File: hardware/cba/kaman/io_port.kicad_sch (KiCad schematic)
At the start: 0 parts

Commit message: hw(schematic): USB to UART circuit for ESP32
With CH340C the UBS to UART for programming the ESP32 is done and it has
the ESD protection with the type C port and the VBUS on USB isn't used
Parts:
- added C10: 100nF, Capacitor_SMD:C_0402_1005Metric_Pad0.74x0.62mm_HandSolder, symbol Device:C
- added C13: 100nF, symbol Device:C
- added J4: USB_C_Receptacle_USB2.0_16P, Connector_USB:USB_C_Receptacle_G-Switch_GT-USB-7010ASV, symbol Connector:USB_C_Receptacle_USB2.0_16P
- added R11, R12: 5.1K, symbol Device:R_US
- added U6: CH340C, Package_SO:SOIC-16_3.9x9.9mm_P1.27mm, symbol Interface_USB:CH340C
- added U7: PRTR5V0U2D, Package_TO_SOT_SMD:SOT-666, symbol Power_Protection:USBLC6-2P6
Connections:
- new net: J4.B5 (CC2), R11.2
- new net: U6.5 (UD+), U7.1 (I/O1)
- new net: U6.6 (UD-), U7.3 (I/O2)
- new net: J4.A6 (D+), J4.B6 (D+), U7.4 (I/O2)
- new net: J4.A7 (D-), J4.B7 (D-), U7.6 (I/O1)
- new net: J4.A4 (VBUS), J4.A9 (VBUS), J4.B4 (VBUS), J4.B9 (VBUS)
- new net: J4.A5 (CC1), R12.2
- new net +3.3V: C10.2, C13.1, U6.16 (VCC), U6.4 (V3), U7.5 (VBUS)
- new net DTR: U6.13 (~{DTR})
- new net GND: C10.1, C13.2, J4.A1 (GND), J4.A12 (GND), J4.B1 (GND), J4.B12 (GND), J4.S1 (SHIELD), R11.1, R12.1, U6.1 (GND), U7.2 (GND)
- new net RTS: U6.14 (~{RTS})
- new net UART RX: U6.2 (TXD)
- new net UART TX: U6.3 (RXD)
- no-connect marks 0 -> 8

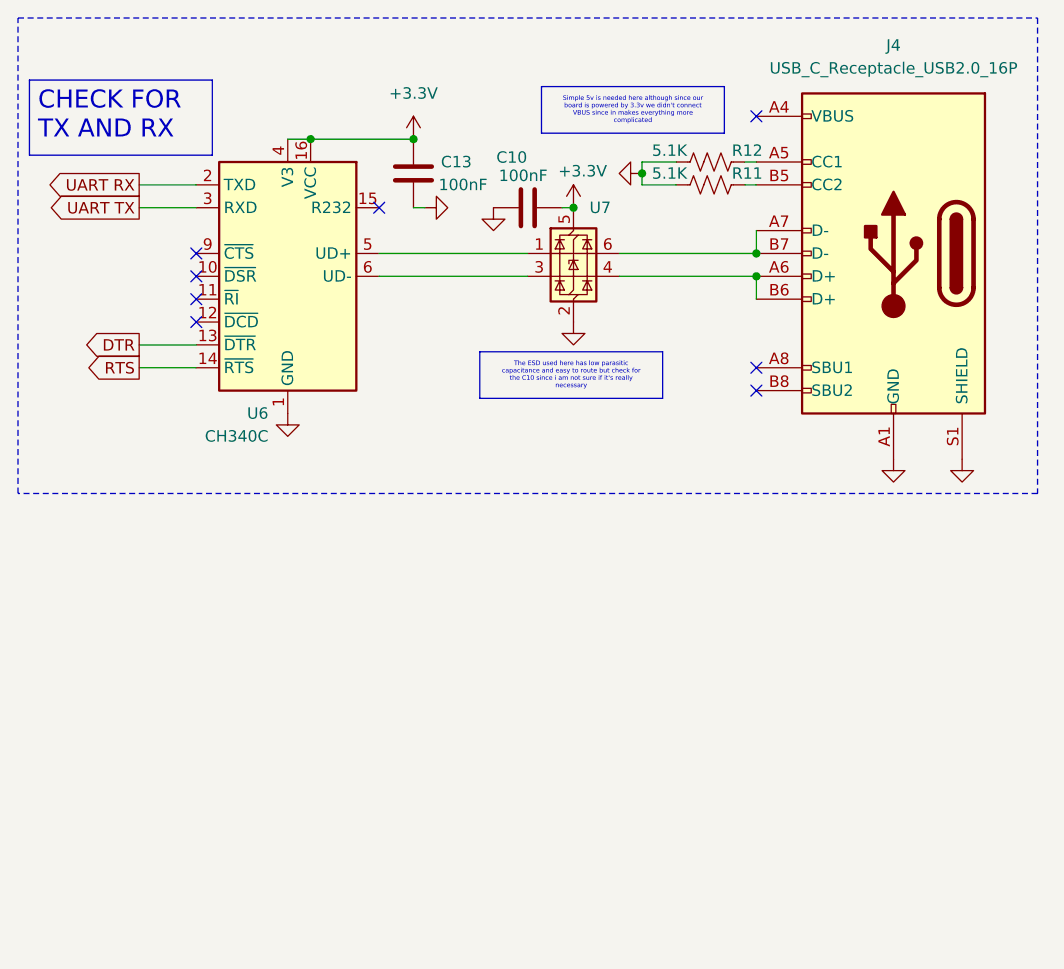
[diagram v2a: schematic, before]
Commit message: hw(schematic): add oled and gps module connector
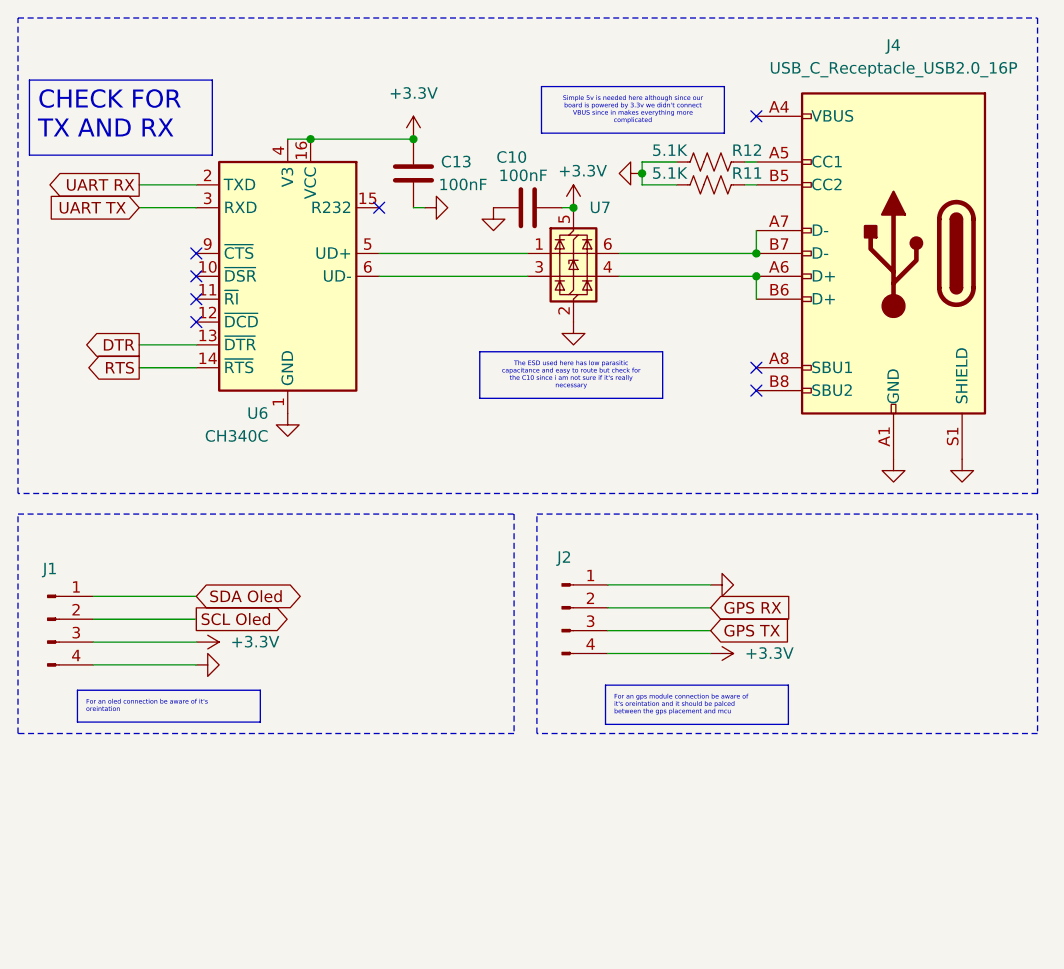
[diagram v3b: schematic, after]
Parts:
- added J1, J2: Conn_01x04_Pin, Connector_PinHeader_2.54mm:PinHeader_1x04_P2.54mm_Vertical, symbol Connector:Conn_01x04_Pin
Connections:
- net +3.3V: now also J1.3 (Pin_3), J2.4 (Pin_4)
- net GND: now also J1.4 (Pin_4), J2.1 (Pin_1)
- new net GPS RX: J2.2 (Pin_2)
- new net GPS TX: J2.3 (Pin_3)
- new net SCL Oled: J1.2 (Pin_2)
- new net SDA Oled: J1.1 (Pin_1)

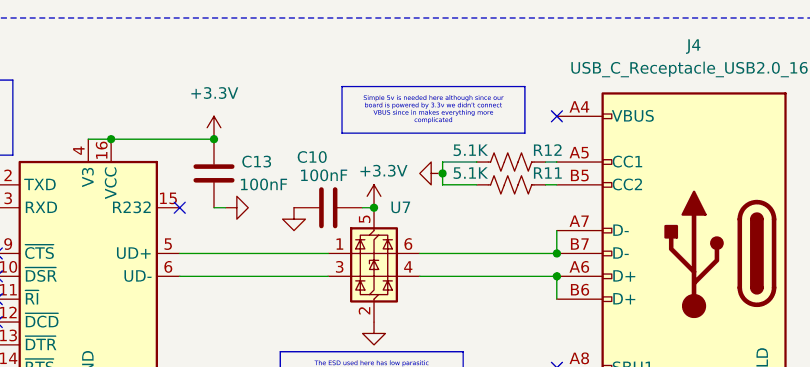
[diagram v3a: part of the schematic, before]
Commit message: hw(schematic): add the power section
Three power sources USB, DC Jack and simple 2.54mm connector with a
schottkey diode on USB and simple ones to block reverse current into a
AZ1117 and outputs 3.3v
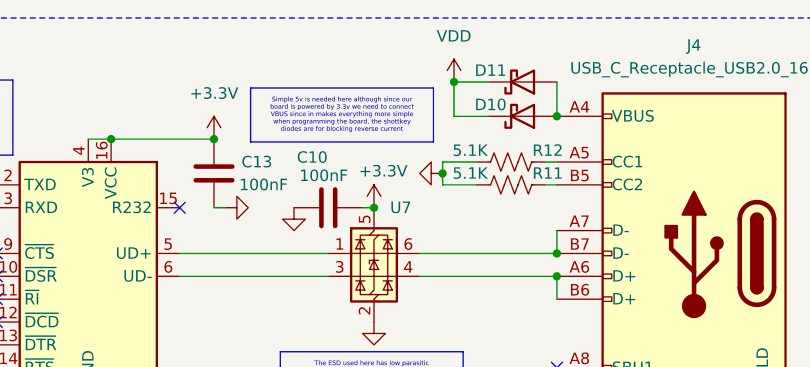
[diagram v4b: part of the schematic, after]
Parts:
- added D10, D11: 1N5819WT, Diode_SMD:D_SOD-523, symbol Diode:1N5819WS
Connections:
- net at J4.A4 (VBUS), J4.A9 (VBUS), J4.B4 (VBUS)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: now also D10.2 (A), D11.2 (A)
- new net VDD: D10.1 (K), D11.1 (K)
- no-connect marks 8 -> 7

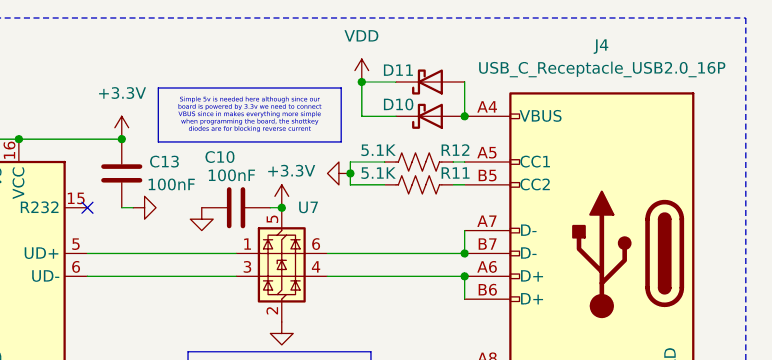
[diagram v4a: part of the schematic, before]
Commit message: hw(schematic): Change reverse current diodes
The previous schottky 1N5819WT is rated for 350mA which needs two for
maximum of 700mA and is repalced with DFLS160-7 which is rated for 1A
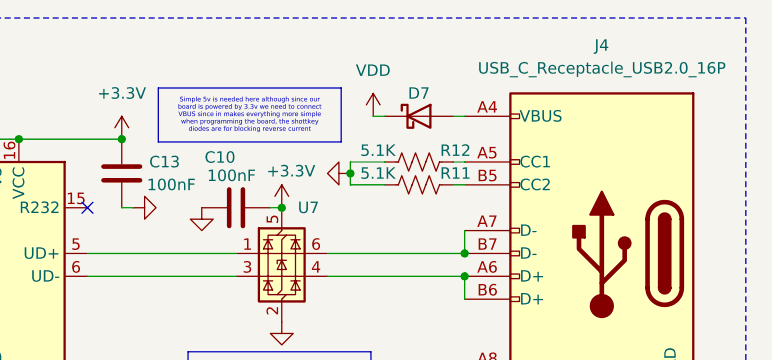
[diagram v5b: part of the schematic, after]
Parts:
- removed D10, D11: 1N5819WT, Diode_SMD:D_SOD-523, symbol Diode:1N5819WS
- added D7: DFLS160-7, Diode_SMD:D_PowerDI-123, symbol Device:D_Schottky
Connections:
- net VDD: now also D7.1 (K)
- net at J4.A4 (VBUS), J4.A9 (VBUS), J4.B4 (VBUS)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: now also D7.2 (A)
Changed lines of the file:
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@@
 	)
 	(junction
-		(at 82.55 19.05)
-		(diameter 0)
-		(color 0 0 0 0)
-	)
-	(junction
 		(at 44.45 25.4)
 		(diameter 0)
@@
 	)
 	(junction
-		(at 93.98 22.86)
-		(diameter 0)
-		(color 0 0 0 0)
-	)
-	(junction
 		(at 93.98 40.64)
 		(diameter 0)
@@
 	(wire
 		(pts
-			(xy 52.07 40.64) (xy 68.58 40.64)
-		)
-		(stroke
-			(width 0)
-			(type default)
-		)
-	)
-	(wire
-		(pts
-			(xy 82.55 22.86) (xy 86.36 22.86)
+			(xy 83.82 22.86) (xy 85.09 22.86)
 		)
 		(stroke
@@
 	(wire
 		(pts
-			(xy 82.55 19.05) (xy 82.55 22.86)
+			(xy 52.07 40.64) (xy 68.58 40.64)
 		)
 		(stroke
@@
 	(wire
 		(pts
-			(xy 82.55 19.05) (xy 86.36 19.05)
-		)
-		(stroke
-			(width 0)
-			(type default)
-		)
-	)
-	(wire
-		(pts
-			(xy 93.98 19.05) (xy 93.98 22.86)
+			(xy 93.98 40.64) (xy 93.98 43.18)
 		)
 		(stroke
@@
 	(wire
 		(pts
-			(xy 93.98 40.64) (xy 93.98 43.18)
+			(xy 92.71 30.48) (xy 93.98 30.48)
 		)
 		(stroke
@@
 	(wire
 		(pts
-			(xy 92.71 30.48) (xy 93.98 30.48)
+			(xy 85.09 30.48) (xy 81.28 30.48)
 		)
 		(stroke
@@
 	(wire
 		(pts
-			(xy 85.09 30.48) (xy 81.28 30.48)
+			(xy 85.09 27.94) (xy 81.28 27.94)
 		)
 		(stroke
@@
 	(wire
 		(pts
-			(xy 85.09 27.94) (xy 81.28 27.94)
+			(xy 72.39 33.02) (xy 73.66 33.02)
 		)
 		(stroke
@@
 	(wire
 		(pts
-			(xy 72.39 33.02) (xy 73.66 33.02)
+			(xy 78.74 38.1) (xy 93.98 38.1)
 		)
 		(stroke
@@
 	(wire
 		(pts
-			(xy 78.74 38.1) (xy 93.98 38.1)
+			(xy 20.32 76.2) (xy 31.75 76.2)
 		)
 		(stroke
@@
 	(wire
 		(pts
-			(xy 20.32 76.2) (xy 31.75 76.2)
+			(xy 92.71 22.86) (xy 93.98 22.86)
 		)
 		(stroke
@@
 	)
 	(symbol
-		(lib_id "Diode:1N5819WS")
-		(at 90.17 19.05 0)
-		(mirror x)
-		(unit 1)
-		(body_style 1)
-		(exclude_from_sim no)
-		(in_bom yes)
-		(on_board yes)
-		(in_pos_files yes)
-		(dnp no)
-		(property "Reference" "D11"
-			(at 86.614 17.78 0)
-			(show_name no)
-			(do_not_autoplace no)
-			(effects
-				(font
-					(size 1.27 1.27)
-				)
-			)
-		)
-		(property "Value" "1N5819WT"
-			(at 89.8525 15.24 0)
-			(hide yes)
-			(show_name no)
-			(do_not_autoplace no)
-			(effects
-				(font
-					(size 1.27 1.27)
-				)
-			)
-		)
-		(property "Footprint" "Diode_SMD:D_SOD-523"
-			(at 90.17 14.605 0)
-			(hide yes)
-			(show_name no)
-			(do_not_autoplace no)
-			(effects
-				(font
-					(size 1.27 1.27)
-				)
-			)
-		)
-		(property "Datasheet" "https://datasheet.lcsc.com/lcsc/2204281430_Guangdong-Hottech-1N5819WS_C191023.pdf"
-			(at 90.17 19.05 0)
-			(hide yes)
-			(show_name no)
-			(do_not_autoplace no)
-			(effects
-				(font
-					(size 1.27 1.27)
-				)
-			)
-		)
-		(property "Description" "40V 600mV@1A 1A SOD-323 Schottky Barrier Diodes, SOD-323"
-			(at 90.17 19.05 0)
-			(hide yes)
-			(show_name no)
-			(do_not_autoplace no)
-			(effects
-				(font
-					(size 1.27 1.27)
-				)
-			)
-		)
-		(pin "1"
-		)
-		(pin "2"
-		)
-		(instances
-			(project "Template"
-				(path "/b7abe575-2b7a-4e47-9046-9769d7102f9d/c3e404eb-2e1f-4ab9-8da3-bc1a9ff0af28/5567a483-a138-4241-99fb-eb385b2c8ebc"
-					(reference "D11")
-					(unit 1)
-				)
-			)
-		)
-	)
-	(symbol
 		(lib_id "Device:C")
 		(at 55.88 29.21 0)
@@
 	)
 	(symbol
+		(lib_id "Device:D_Schottky")
+		(at 88.9 22.86 0)
+		(unit 1)
+		(body_style 1)
+		(exclude_from_sim no)
+		(in_bom yes)
+		(on_board yes)
+		(in_pos_files yes)
+		(dnp no)
+		(property "Reference" "D7"
+			(at 88.9 20.32 0)
+			(show_name no)
+			(do_not_autoplace no)
+			(effects
+				(font
+					(size 1.27 1.27)
+				)
+			)
+		)
+		(property "Value" "DFLS160-7"
+			(at 88.5825 19.05 0)
+			(hide yes)
+			(show_name no)
+			(do_not_autoplace no)
+			(effects
+				(font
+					(size 1.27 1.27)
+				)
+			)
+		)
+		(property "Footprint" "Diode_SMD:D_PowerDI-123"
+			(at 88.9 22.86 0)
+			(hide yes)
+			(show_name no)
+			(do_not_autoplace no)
+			(effects
+				(font
+					(size 1.27 1.27)
+				)
+			)
+		)
+		(property "Datasheet" ""
+			(at 88.9 22.86 0)
+			(hide yes)
+			(show_name no)
+			(do_not_autoplace no)
+			(effects
+				(font
+					(size 1.27 1.27)
+				)
+			)
+		)
+		(property "Description" "Schottky diode"
+			(at 88.9 22.86 0)
+			(hide yes)
+			(show_name no)
+			(do_not_autoplace no)
+			(effects
+				(font
+					(size 1.27 1.27)
+				)
+			)
+		)
+		(pin "2"
+		)
+		(pin "1"
+		)
+		(instances
+			(project "Template"
+				(path "/b7abe575-2b7a-4e47-9046-9769d7102f9d/c3e404eb-2e1f-4ab9-8da3-bc1a9ff0af28/5567a483-a138-4241-99fb-eb385b2c8ebc"
+					(reference "D7")
+					(unit 1)
+				)
+			)
+		)
+	)
+	(symbol
 		(lib_id "power:VDD")
-		(at 82.55 19.05 0)
+		(at 83.82 22.86 0)
 		(unit 1)
 		(body_style 1)
@@
 		(fields_autoplaced yes)
 		(property "Reference" "#PWR038"
-			(at 82.55 22.86 0)
+			(at 83.82 26.67 0)
 			(hide yes)
 			(show_name no)
@@
 		)
 		(property "Value" "VDD"
-			(at 82.55 13.97 0)
+			(at 83.82 17.78 0)
 			(show_name no)
 			(do_not_autoplace no)
@@
 		)
 		(property "Footprint" ""
-			(at 82.55 19.05 0)
+			(at 83.82 22.86 0)
 			(hide yes)
 			(show_name no)
@@
 		)
 		(property "Datasheet" ""
-			(at 82.55 19.05 0)
+			(at 83.82 22.86 0)
 			(hide yes)
 			(show_name no)
@@
 		)
 		(property "Description" "Power symbol creates a global label with name \"VDD\""
-			(at 82.55 19.05 0)
+			(at 83.82 22.86 0)
 			(hide yes)
 			(show_name no)
@@
 					(unit 1)
 				)
-			)
-		)
-	)
-	(symbol
-		(lib_id "Diode:1N5819WS")
-		(at 90.17 22.86 0)
-		(mirror x)
-		(unit 1)
-		(body_style 1)
-		(exclude_from_sim no)
-		(in_bom yes)
-		(on_board yes)
-		(in_pos_files yes)
-		(dnp no)
-		(property "Reference" "D10"
-			(at 86.614 21.59 0)
-			(show_name no)
-			(do_not_autoplace no)
-			(effects
-				(font
-					(size 1.27 1.27)
-				)
-			)
-		)
-		(property "Value" "1N5819WT"
-			(at 89.8525 19.05 0)
-			(hide yes)
-			(show_name no)
-			(do_not_autoplace no)
-			(effects
-				(font
-					(size 1.27 1.27)
-				)
-			)
-		)
-		(property "Footprint" "Diode_SMD:D_SOD-523"
-			(at 90.17 18.415 0)
-			(hide yes)
-			(show_name no)
-			(do_not_autoplace no)
-			(effects
-				(font
-					(size 1.27 1.27)
-				)
-			)
-		)
-		(property "Datasheet" "https://datasheet.lcsc.com/lcsc/2204281430_Guangdong-Hottech-1N5819WS_C191023.pdf"
-			(at 90.17 22.86 0)
-			(hide yes)
-			(show_name no)
-			(do_not_autoplace no)
-			(effects
-				(font
-					(size 1.27 1.27)
-				)
-			)
-		)
-		(property "Description" "40V 600mV@1A 1A SOD-323 Schottky Barrier Diodes, SOD-323"
-			(at 90.17 22.86 0)
-			(hide yes)
-			(show_name no)
-			(do_not_autoplace no)
-			(effects
-				(font
-					(size 1.27 1.27)
-				)
-			)
-		)
-		(pin "1"
-		)
-		(pin "2"
-		)
-		(instances
-			(project "Template"
-				(path "/b7abe575-2b7a-4e47-9046-9769d7102f9d/c3e404eb-2e1f-4ab9-8da3-bc1a9ff0af28/5567a483-a138-4241-99fb-eb385b2c8ebc"
-					(reference "D10")
-					(unit 1)
-				)

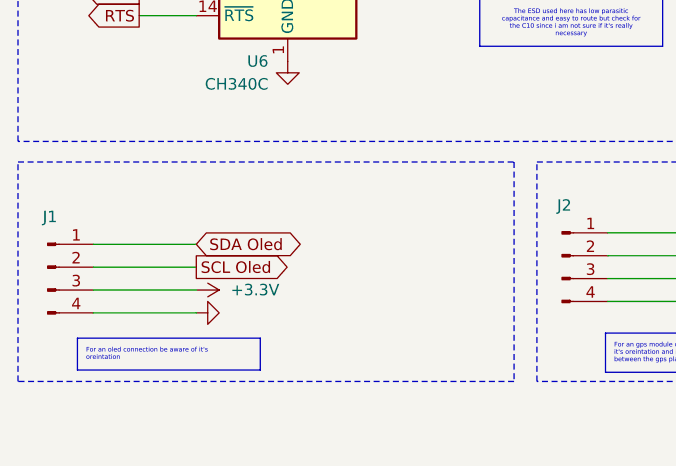
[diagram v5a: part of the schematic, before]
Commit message: hw(schematic): add pullup resistors to oled I2C
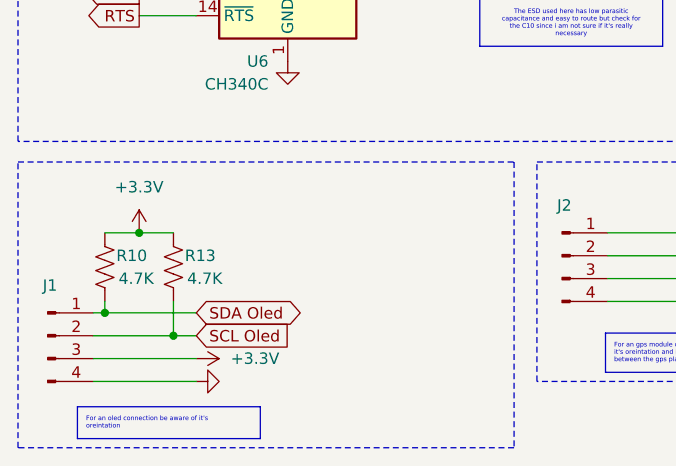
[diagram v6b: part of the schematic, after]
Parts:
- added R10, R13: 4.7K, Capacitor_SMD:C_0603_1608Metric_Pad1.08x0.95mm_HandSolder, symbol Device:R_US
- C13, R11, R12: footprint (none) -> Capacitor_SMD:C_0603_1608Metric_Pad1.08x0.95mm_HandSolder
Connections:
- net +3.3V: now also R10.1, R13.1
- net SCL Oled: now also R13.2
- net SDA Oled: now also R10.2
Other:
- moved on the sheet: J1

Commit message: hw(pcb): add missing 3d models for parts
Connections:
- net GND: now also J4.SH (SHIELD); no longer J4.S1 (SHIELD)
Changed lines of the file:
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@@
 		(pin "B12"
 		)
-		(pin "S1"
+		(pin "SH"
 		)
 		(pin "A4"
